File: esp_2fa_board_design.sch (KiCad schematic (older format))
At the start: 38 parts, among them IC1 TPS22919DCKR, J1 Conn_01x06_Female, J2 TYPE-C-31-M-17, Q1 DMP2305U-7, SW1 SW_Push, SW2 SW_Push, SW3 BOOT, SW4 RESET, U1 ESP32-WROOM-32, U2 DS3231M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

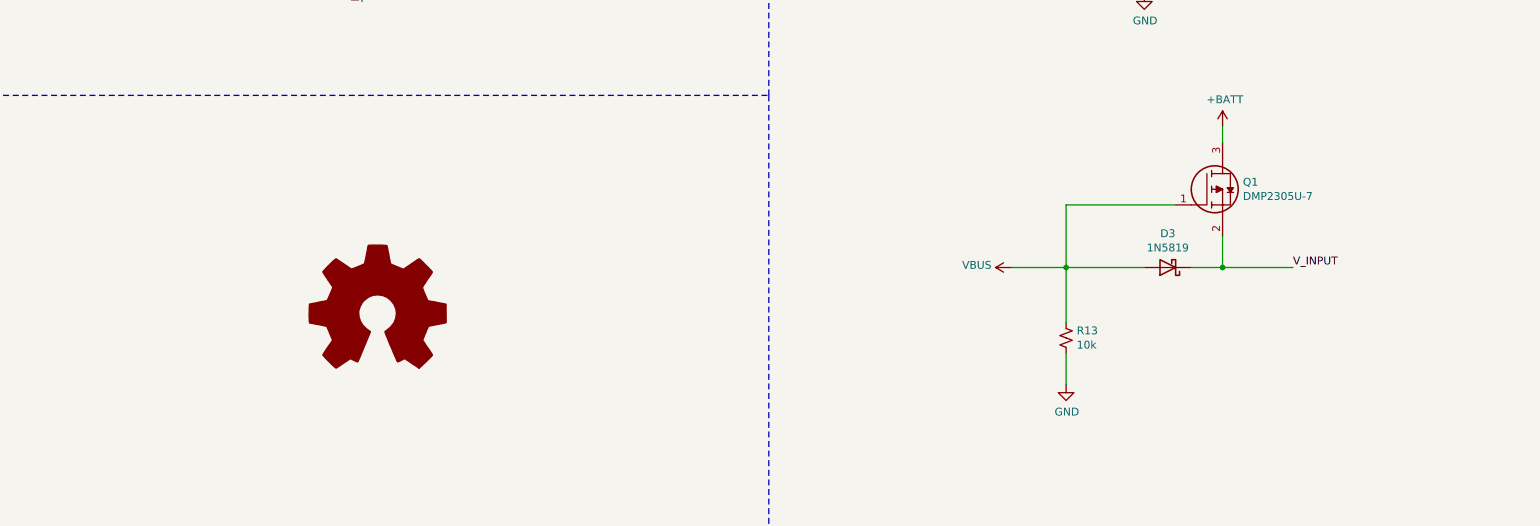
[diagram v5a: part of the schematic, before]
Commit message: Completed PCB routing
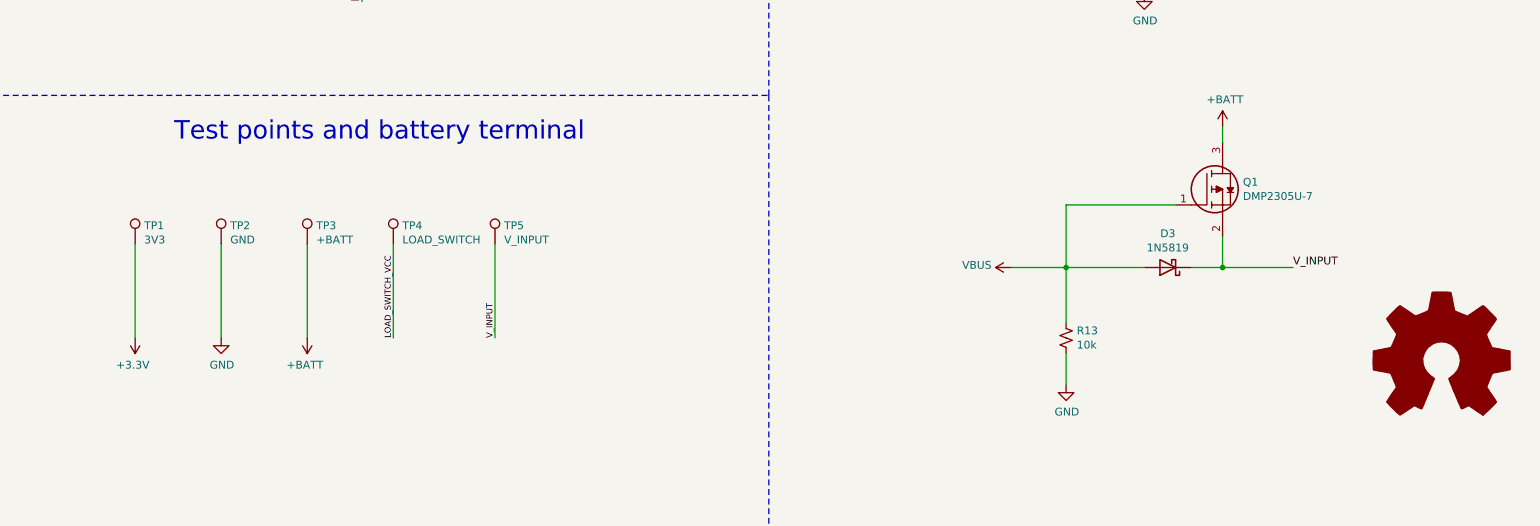
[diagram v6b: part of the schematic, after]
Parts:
- added TP1: 3V3, Connector_Wire:SolderWirePad_1x01_SMD_1x2mm, symbol Connector:TestPoint
- added TP2: GND, Connector_Wire:SolderWirePad_1x01_SMD_1x2mm, symbol Connector:TestPoint
- added TP3: +BATT, Connector_Wire:SolderWirePad_1x01_SMD_1x2mm, symbol Connector:TestPoint
- added TP4: LOAD_SWITCH, Connector_Wire:SolderWirePad_1x01_SMD_1x2mm, symbol Connector:TestPoint
- added TP5: V_INPUT, Connector_Wire:SolderWirePad_1x01_SMD_1x2mm, symbol Connector:TestPoint
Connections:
- net +3V3: now also TP1.1
- net +BATT: now also TP3.1
- net GND: now also TP2.1
- net LOAD_SWITCH_VCC: now also TP4.1
- net V_INPUT: now also TP5.1
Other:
- note added: "Test points and battery terminal"
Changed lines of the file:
@@
 	6050 7700 6050 11150
-$Comp
-L esp_2fa_board_design-rescue:Logo_Open_Hardware_Large-Graphic #LOGO1
-U 1 1 5FB5EB94
-P 8650 9100
-F 0 "#LOGO1" H 8650 9600 50  0001 C CNN
-F 1 "Logo_Open_Hardware_Large" H 8650 8700 50  0001 C CNN
-F 2 "" H 8650 9100 50  0001 C CNN
-F 3 "~" H 8650 9100 50  0001 C CNN
-	1    8650 9100
-	1    0    0    -1
-$EndComp
 $Comp
 L esp_2fa_board_design-rescue:GND-power #PWR024
@@
 Connection ~ 1900 9100
 Connection ~ 1900 9200
+$Comp
+L esp_2fa_board_design-rescue:Logo_Open_Hardware_Large-Graphic #LOGO1
+U 1 1 5FB5EB94
+P 15450 9400
+F 0 "#LOGO1" H 15450 9900 50  0001 C CNN
+F 1 "Logo_Open_Hardware_Large" H 15450 9000 50  0001 C CNN
+F 2 "" H 15450 9400 50  0001 C CNN
+F 3 "~" H 15450 9400 50  0001 C CNN
+	1    15450 9400
+	1    0    0    -1
+$EndComp
+$Comp
+L Connector:TestPoint TP1
+U 1 1 5FBDE92D
+P 7100 8650
+F 0 "TP1" H 7158 8768 50  0000 L CNN
+F 1 "3V3" H 7158 8677 50  0000 L CNN
+F 2 "Connector_Wire:SolderWirePad_1x01_SMD_1x2mm" H 7300 8650 50  0001 C CNN
+F 3 "~" H 7300 8650 50  0001 C CNN
+	1    7100 8650
+	1    0    0    -1
+$EndComp
+$Comp
+L Connector:TestPoint TP2
+U 1 1 5FBE1246
+P 7650 8650
+F 0 "TP2" H 7708 8768 50  0000 L CNN
+F 1 "GND" H 7708 8677 50  0000 L CNN
+F 2 "Connector_Wire:SolderWirePad_1x01_SMD_1x2mm" H 7850 8650 50  0001 C CNN
+F 3 "~" H 7850 8650 50  0001 C CNN
+	1    7650 8650
+	1    0    0    -1
+$EndComp
+$Comp
+L Connector:TestPoint TP3
+U 1 1 5FBE142E
+P 8200 8650
+F 0 "TP3" H 8258 8768 50  0000 L CNN
+F 1 "+BATT" H 8258 8677 50  0000 L CNN
+F 2 "Connector_Wire:SolderWirePad_1x01_SMD_1x2mm" H 8400 8650 50  0001 C CNN
+F 3 "~" H 8400 8650 50  0001 C CNN
+	1    8200 8650
+	1    0    0    -1
+$EndComp
+$Comp
+L Connector:TestPoint TP4
+U 1 1 5FBE16FC
+P 8750 8650
+F 0 "TP4" H 8808 8768 50  0000 L CNN
+F 1 "LOAD_SWITCH" H 8808 8677 50  0000 L CNN
+F 2 "Connector_Wire:SolderWirePad_1x01_SMD_1x2mm" H 8950 8650 50  0001 C CNN
+F 3 "~" H 8950 8650 50  0001 C CNN
+	1    8750 8650
+	1    0    0    -1
+$EndComp
+$Comp
+L Connector:TestPoint TP5
+U 1 1 5FBE1988
+P 9400 8650
+F 0 "TP5" H 9458 8768 50  0000 L CNN
+F 1 "V_INPUT" H 9458 8677 50  0000 L CNN
+F 2 "Connector_Wire:SolderWirePad_1x01_SMD_1x2mm" H 9600 8650 50  0001 C CNN
+F 3 "~" H 9600 8650 50  0001 C CNN
+	1    9400 8650
+	1    0    0    -1
+$EndComp
+Text Notes 7350 8000 0    118  ~ 0
+Test points and battery terminal
+Wire Wire Line
+	7100 8650 7100 9250
+Wire Wire Line
+	7650 8650 7650 9250
+Wire Wire Line
+	8200 8650 8200 9250
+Wire Wire Line
+	8750 8650 8750 9250
+Wire Wire Line
+	9400 8650 9400 9250
+$Comp
+L power:+3.3V #PWR030
+U 1 1 5FC0B82F
+P 7100 9250
+F 0 "#PWR030" H 7100 9100 50  0001 C CNN
+F 1 "+3.3V" H 7115 9423 50  0000 C CNN
+F 2 "" H 7100 9250 50  0001 C CNN
+F 3 "" H 7100 9250 50  0001 C CNN
+	1    7100 9250
+	-1   0    0    1
+$EndComp
+$Comp
+L power:GND #PWR031
+U 1 1 5FC0BC1F
+P 7650 9250
+F 0 "#PWR031" H 7650 9000 50  0001 C CNN
+F 1 "GND" H 7655 9077 50  0000 C CNN
+F 2 "" H 7650 9250 50  0001 C CNN
+F 3 "" H 7650 9250 50  0001 C CNN
+	1    7650 9250
+	1    0    0    -1
+$EndComp
+$Comp
+L power:+BATT #PWR032
+U 1 1 5FC0BFDD
+P 8200 9250
+F 0 "#PWR032" H 8200 9100 50  0001 C CNN
+F 1 "+BATT" H 8215 9423 50  0000 C CNN
+F 2 "" H 8200 9250 50  0001 C CNN
+F 3 "" H 8200 9250 50  0001 C CNN
+	1    8200 9250
+	-1   0    0    1
+$EndComp
+Text Label 8750 9250 1    39   ~ 0
+LOAD_SWITCH_VCC
+Text Label 9400 9250 1    39   ~ 0
+V_INPUT
 $EndSCHEMATC

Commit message: Updated schematics according review feedback
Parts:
- added C1: 10uF 50V, Capacitor_SMD:C_1206_3216Metric, symbol esp_2fa_board_design-rescue:C-Device
- added C10: 1uF 50V, Capacitor_SMD:C_1206_3216Metric, symbol esp_2fa_board_design-rescue:C-Device
- added C2: 0.1uF 50V, Capacitor_SMD:C_1206_3216Metric, symbol esp_2fa_board_design-rescue:C-Device
- added J3: Conn_01x02_Male, Connector_PinHeader_1.27mm:PinHeader_1x01_P1.27mm_Horizontal, symbol Connector:Conn_01x02_Male
- added TP6: OLED_SDA, Connector_Wire:SolderWirePad_1x01_SMD_1x2mm, symbol Connector:TestPoint
- added TP7: OLED_SCL, Connector_Wire:SolderWirePad_1x01_SMD_1x2mm, symbol Connector:TestPoint
- added TP8: GND, Connector_Wire:SolderWirePad_1x01_SMD_1x2mm, symbol Connector:TestPoint
- C3, C5: value 1uF -> 1uF 50V
- C4, C6, C8, C9: value 10uF -> 10uF 50V
- C7: value 0.1uF -> 0.1uF 50V
- TP2: value GND -> RTC_SDA
- TP3: value +BATT -> RTC_SCL
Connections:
- net +3V3: now also C1.1, C2.2
- net +BATT: now also J3.1 (Pin_1); no longer TP3.1
- net GND: now also C1.2, C10.2, C2.1, J3.2 (Pin_2), TP8.1; no longer TP2.1
- net IO18_SCL: now also TP3.1
- net IO21_SDA: now also TP6.1
- net IO22_SCL: now also TP7.1
- net IO5_SDA: now also TP2.1
- net at BT1.1 (+), U2.14 (VBAT): now also C10.1
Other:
- note added: "HIGH - Charge complete state\nLOW - Charging state"
- note added: "I_REG = 1000/R_PROG\n\nWhere:\nR_PROG = kOhms\nI_REG = milliampere"
- note added: "Test points"
- note removed: "Test points and battery terminal"
- moved on the sheet: R10, R9, TP1, TP4, TP5, U1

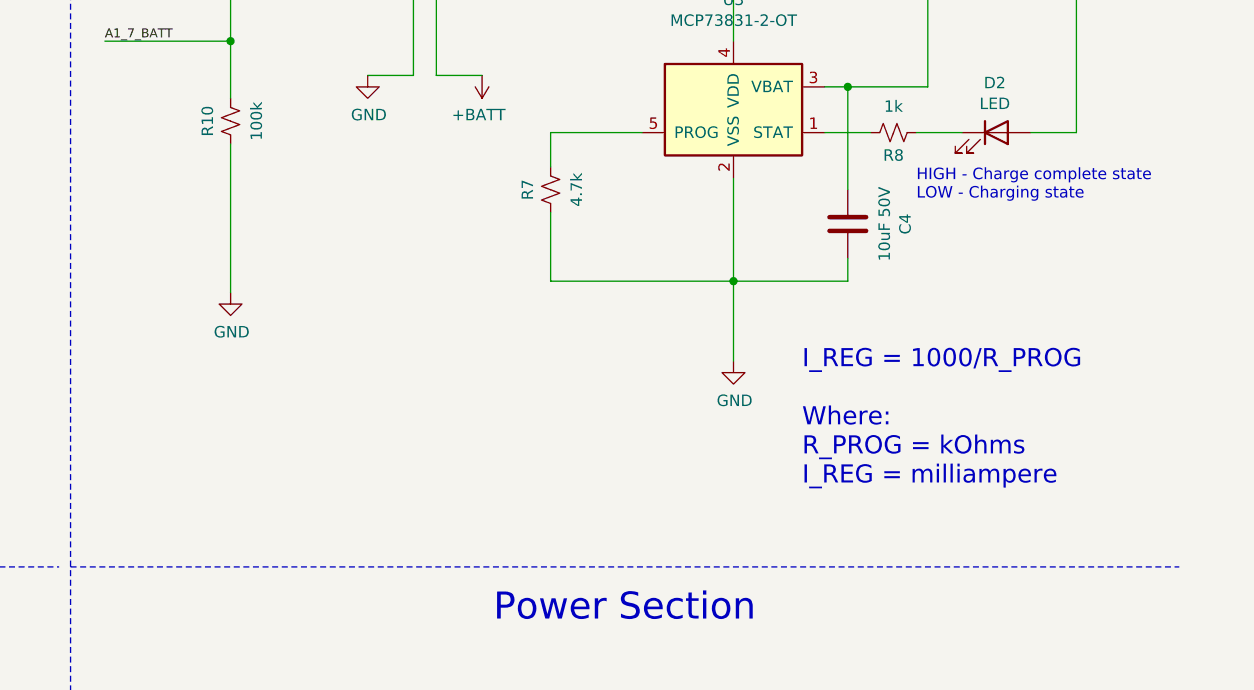
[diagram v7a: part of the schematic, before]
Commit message: Updated schematics to add lipo output current
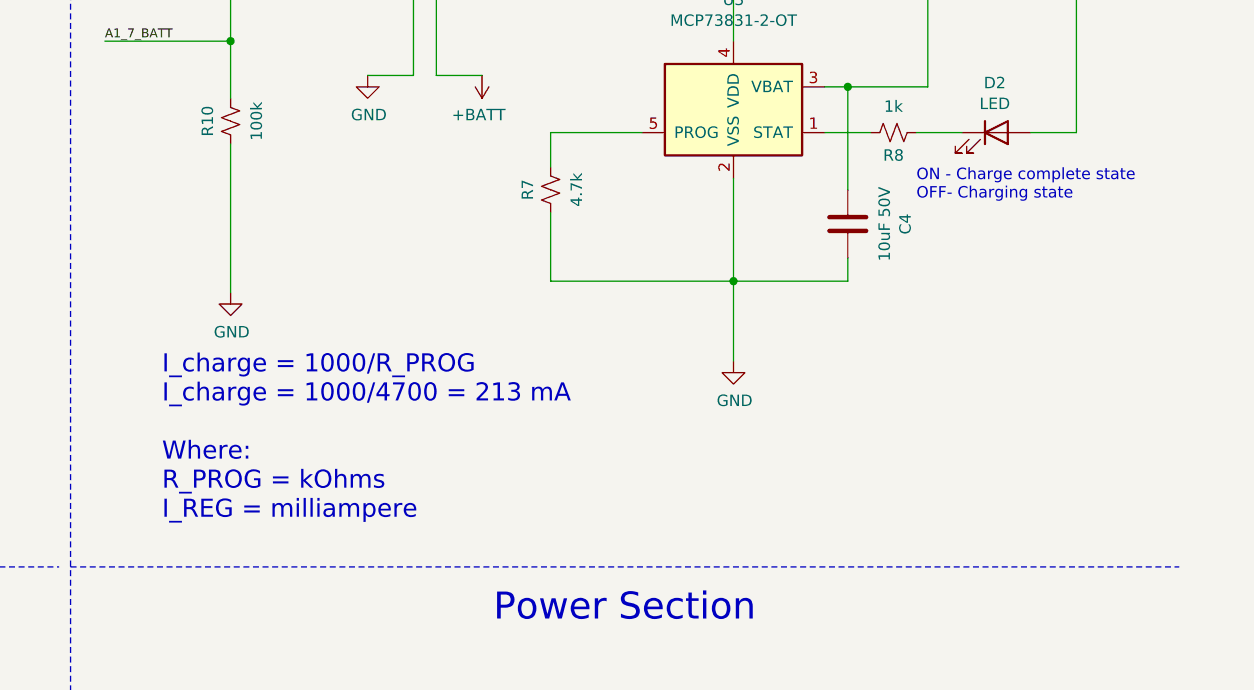
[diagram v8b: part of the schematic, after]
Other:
- note added: "I_charge = 1000/R_PROG\nI_charge = 1000/4700 = 213 mA\n\nWhere:\nR_PROG = kOhms\nI_REG = milliampere"
- note added: "ON - Charge complete state\nOFF- Charging state"
- note removed: "HIGH - Charge complete state\nLOW - Charging state"
- note removed: "I_REG = 1000/R_PROG\n\nWhere:\nR_PROG = kOhms\nI_REG = milliampere"
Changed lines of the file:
@@
 	3100 1150 3100 1300
 Text Notes 14850 2700 0    50   ~ 0
-HIGH - Charge complete state\nLOW - Charging state
-Text Notes 14350 3950 0    79   ~ 0
-I_REG = 1000/R_PROG\n\nWhere:\nR_PROG = kOhms\nI_REG = milliampere
+ON - Charge complete state\nOFF- Charging state
+Text Notes 11550 4100 0    79   ~ 0
+I_charge = 1000/R_PROG\nI_charge = 1000/4700 = 213 mA\n\nWhere:\nR_PROG = kOhms\nI_REG = milliampere
 Wire Wire Line
 	3950 8900 3950 9200
